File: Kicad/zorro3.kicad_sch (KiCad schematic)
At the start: 13 parts, among them CN1 Zorro3, U1 SN74ABT16543DGGR, U12 74LVC07APW_118, U13 SN74ABT16245ADGGR, U2 SN74ABT16543DGGR, U3 SN74ABT16543DGGR, U6 SN74ABT16543DGGR

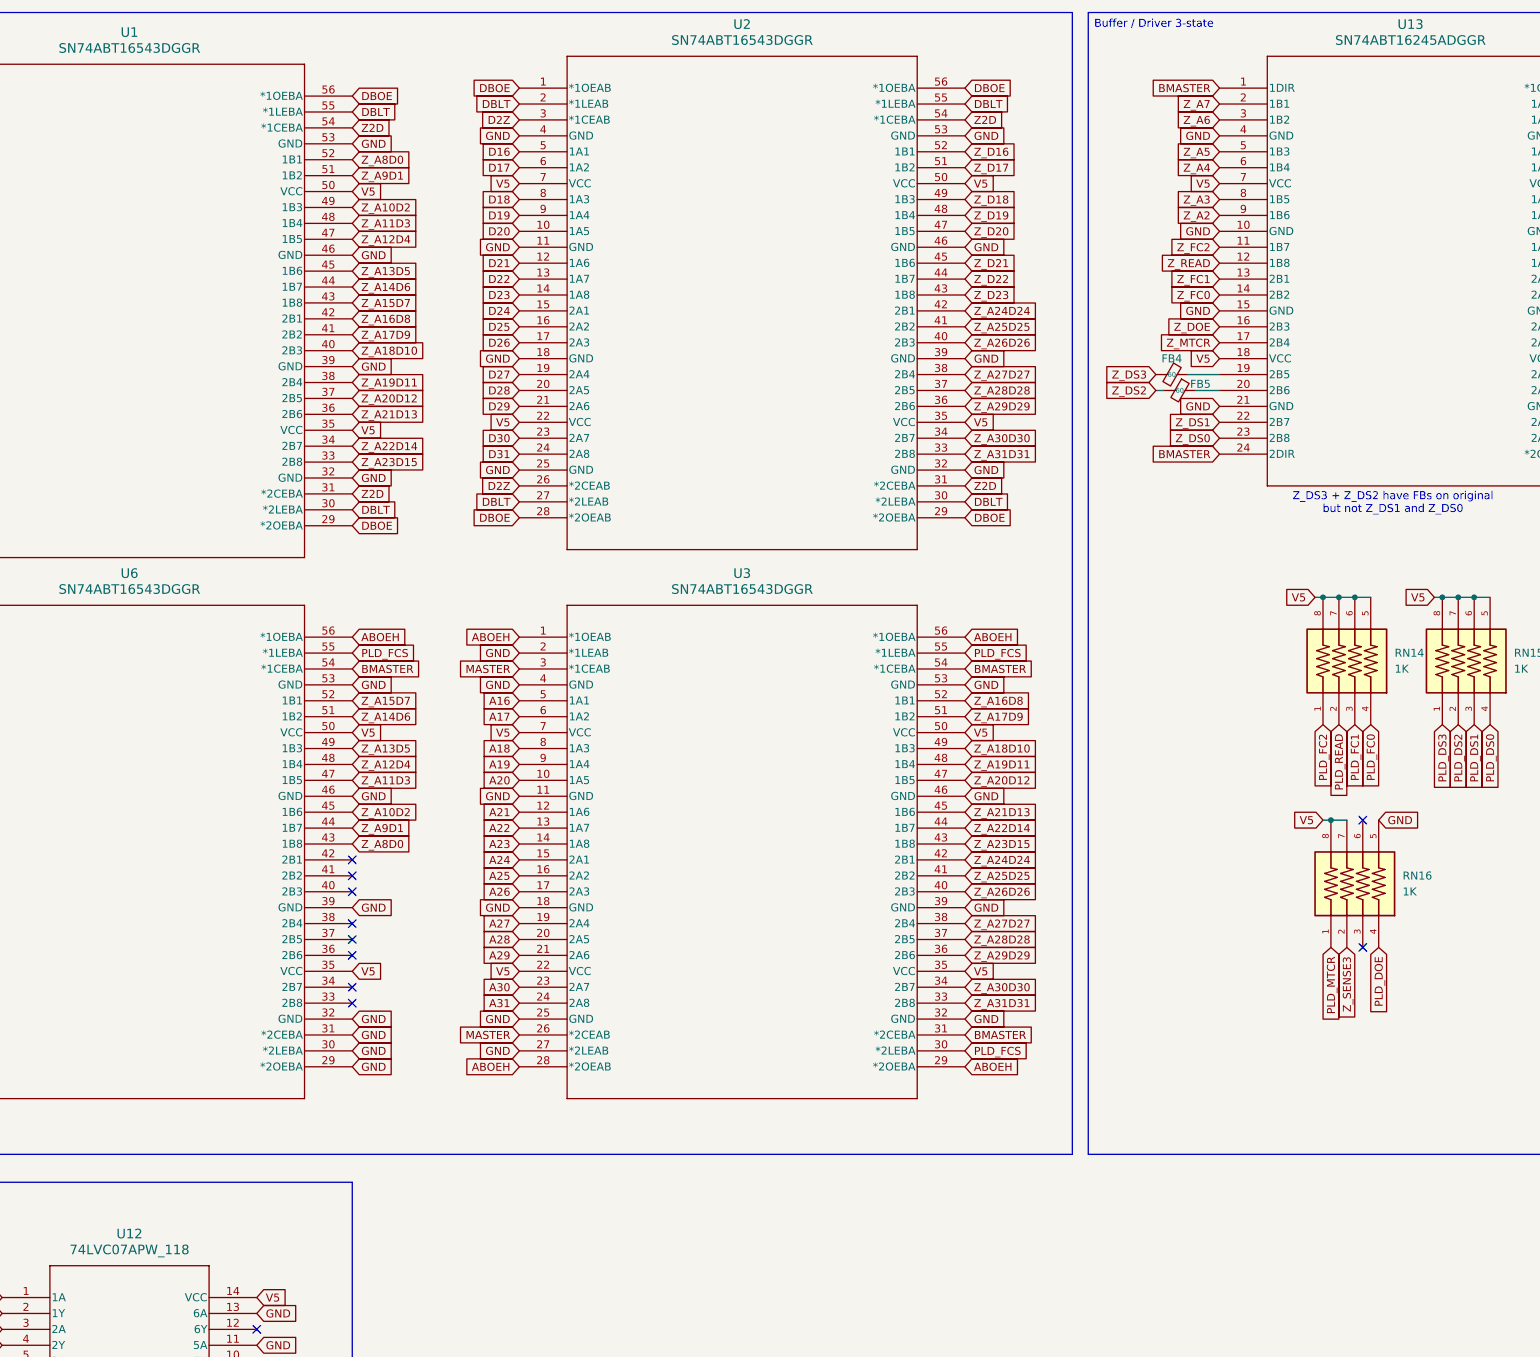
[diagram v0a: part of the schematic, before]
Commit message: Rename all Uxx parts from U1 to U13 for consistency
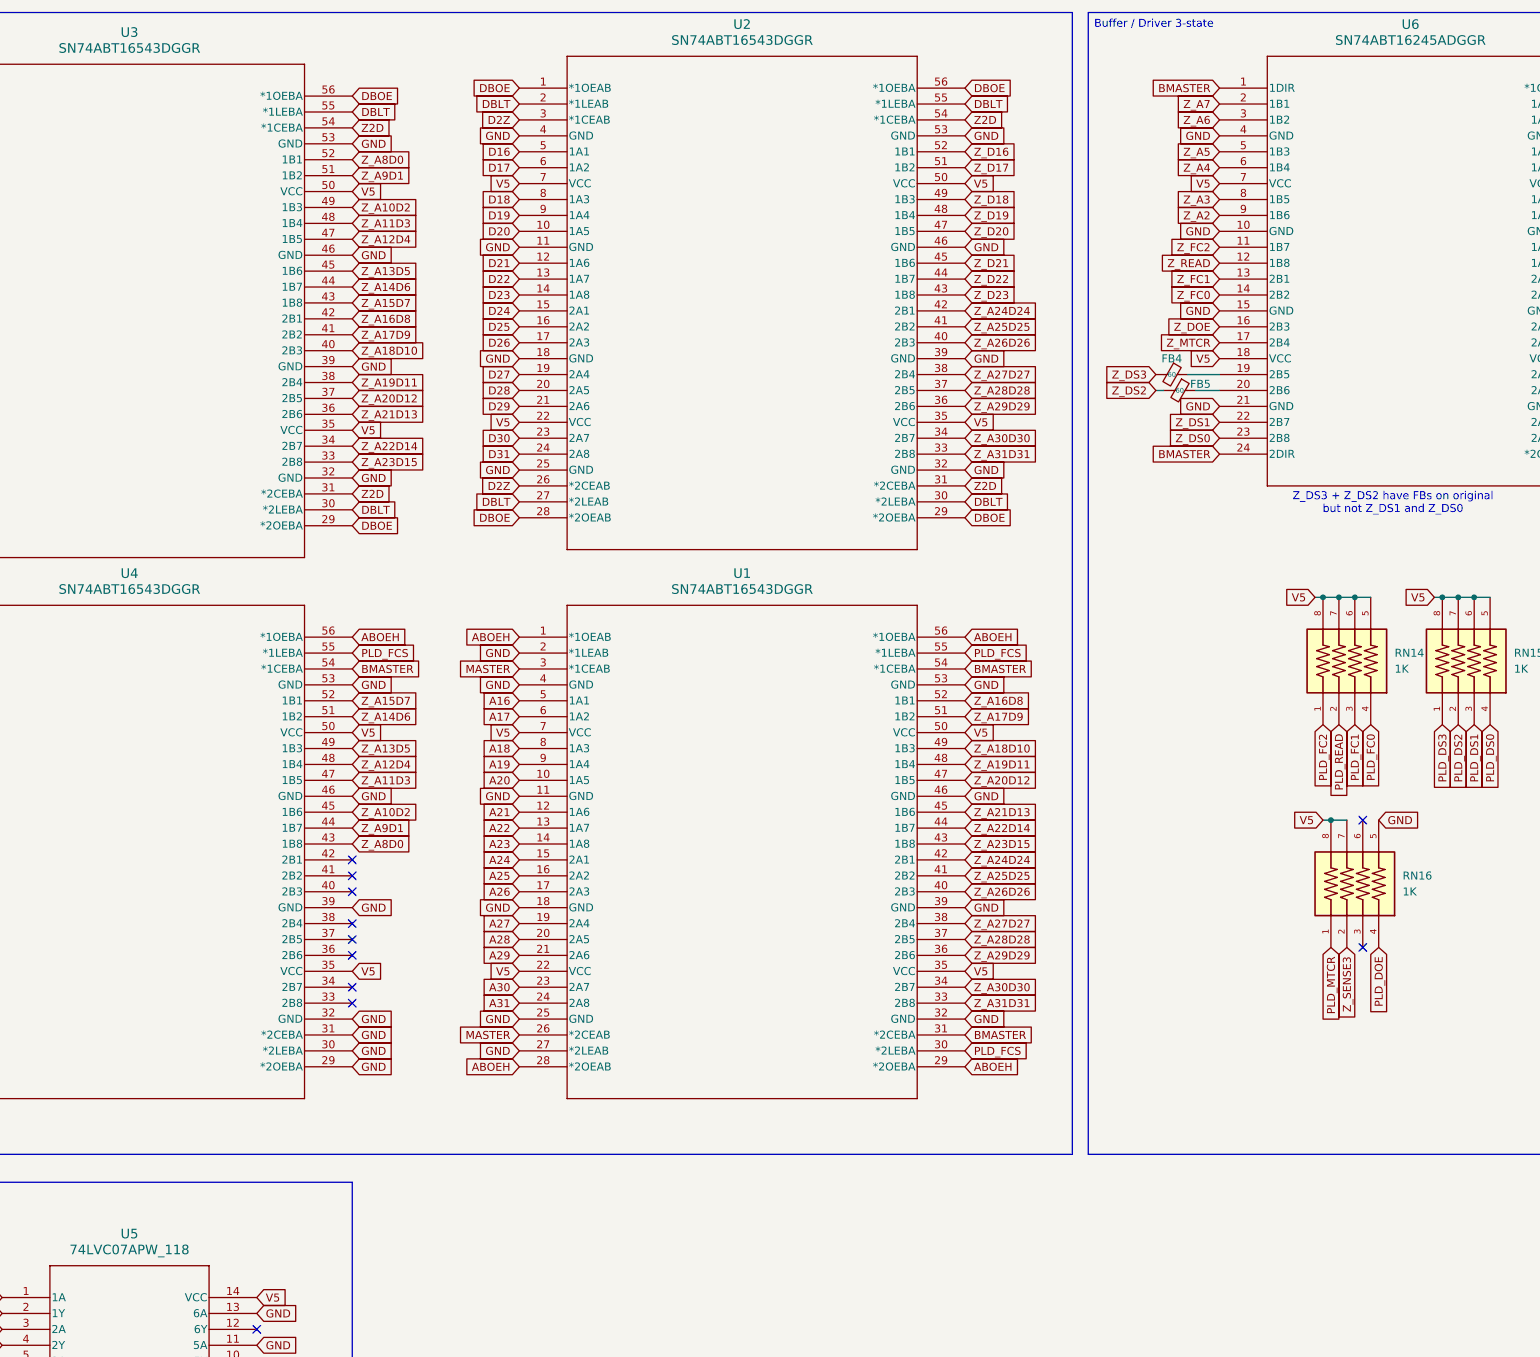
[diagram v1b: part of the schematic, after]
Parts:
- renumbered U3 to U1, U1 to U3, U6 to U4, U12 to U5, U13 to U6
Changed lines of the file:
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@@
 		(dnp no)
 		(fields_autoplaced yes)
-		(property "Reference" "U3"
+		(property "Reference" "U1"
 			(at 161.29 104.14 0)
 			(effects
@@
 			(project ""
 				(path "/8f9f4021-47aa-41d9-bea7-f6ccf72098bb/54ff82a5-3c96-49ab-8139-25683e385401"
-					(reference "U3")
+					(reference "U1")
 					(unit 1)
 				)
@@
 		(dnp no)
 		(fields_autoplaced yes)
-		(property "Reference" "U1"
+		(property "Reference" "U3"
 			(at 63.5 17.78 0)
 			(effects
@@
 			(project ""
 				(path "/8f9f4021-47aa-41d9-bea7-f6ccf72098bb/54ff82a5-3c96-49ab-8139-25683e385401"
-					(reference "U1")
+					(reference "U3")
 					(unit 1)
 				)
@@
 		(dnp no)
 		(fields_autoplaced yes)
-		(property "Reference" "U6"
+		(property "Reference" "U4"
 			(at 63.5 104.14 0)
 			(effects
@@
 			(project "A4092"
 				(path "/8f9f4021-47aa-41d9-bea7-f6ccf72098bb/54ff82a5-3c96-49ab-8139-25683e385401"
-					(reference "U6")
+					(reference "U4")
 					(unit 1)
 				)
@@
 		(dnp no)
 		(fields_autoplaced yes)
-		(property "Reference" "U12"
+		(property "Reference" "U5"
 			(at 63.5 209.55 0)
 			(effects
@@
 			(project ""
 				(path "/8f9f4021-47aa-41d9-bea7-f6ccf72098bb/54ff82a5-3c96-49ab-8139-25683e385401"
-					(reference "U12")
+					(reference "U5")
 					(unit 1)
 				)
@@
 		(dnp no)
 		(fields_autoplaced yes)
-		(property "Reference" "U13"
+		(property "Reference" "U6"
 			(at 267.97 16.51 0)
 			(effects
@@
 			(project ""
 				(path "/8f9f4021-47aa-41d9-bea7-f6ccf72098bb/54ff82a5-3c96-49ab-8139-25683e385401"
-					(reference "U13")
+					(reference "U6")
 					(unit 1)
 				)

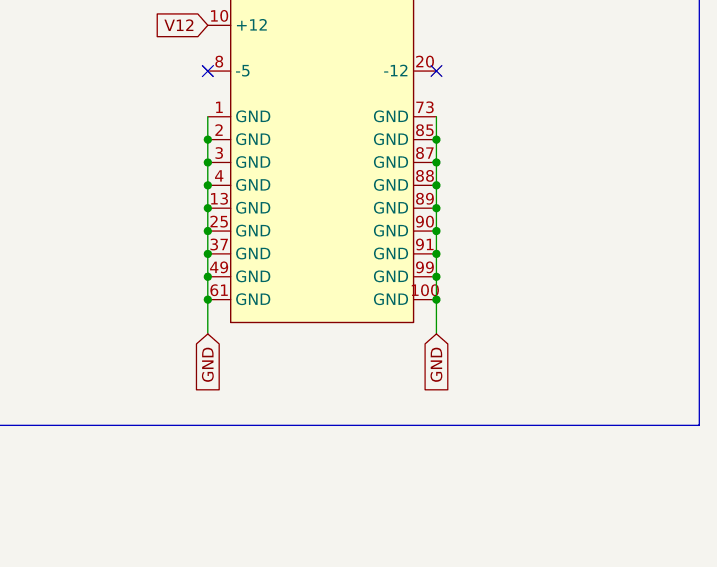
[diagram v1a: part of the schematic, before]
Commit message: Fix Zorro III symbol
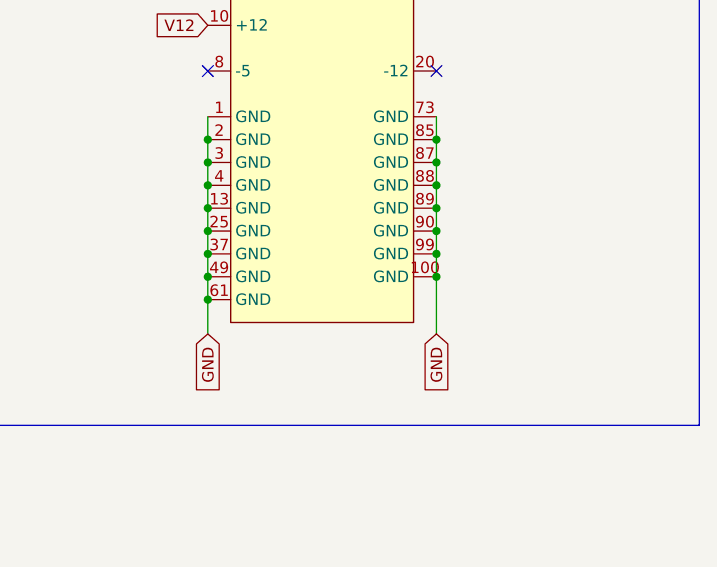
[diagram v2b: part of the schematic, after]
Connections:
- net GND: no longer CN1.91 (GND)
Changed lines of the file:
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@@
 	)
 	(junction
-		(at 370.84 182.88)
-		(diameter 0)
-		(color 0 0 0 0)
-	)
-	(junction
 		(at 370.84 172.72)
 		(diameter 0)
@@
 	(wire
 		(pts
-			(xy 370.84 182.88) (xy 370.84 186.69)
-		)
-		(stroke
-			(width 0)
-			(type default)
-		)
-	)
-	(wire
-		(pts
 			(xy 345.44 180.34) (xy 345.44 182.88)
 		)
@@
 	(wire
 		(pts
-			(xy 370.84 180.34) (xy 370.84 182.88)
+			(xy 370.84 180.34) (xy 370.84 186.69)
 		)
 		(stroke
@@
 	)
 	(symbol
+		(lib_name "Zorro3_1")
 		(lib_id "Zorro3:Zorro3")
 		(at 358.14 166.37 0)
@@
 		(pin "96"
 		)
-		(pin "91"
-		)
 		(pin "36"

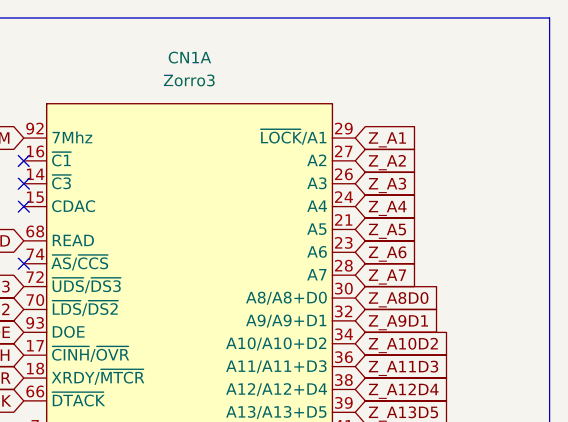
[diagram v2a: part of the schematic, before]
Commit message: Fix Z_LOCK in zorro3 schematics
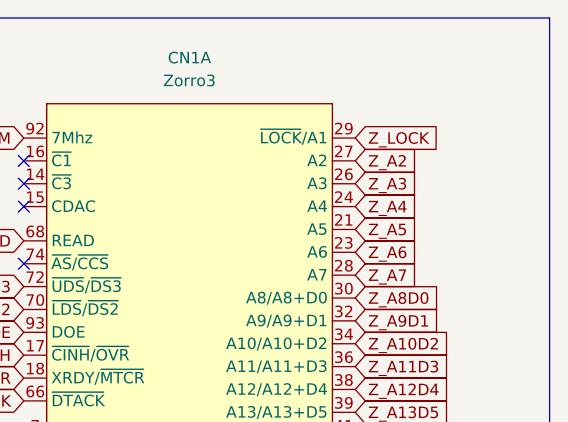
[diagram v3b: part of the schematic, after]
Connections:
- net Z_A1 renamed Z_LOCK
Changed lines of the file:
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@@
 		)
 	)
-	(global_label "Z_A1"
+	(global_label "Z_LOCK"
 		(shape input)
 		(at 378.46 27.94 0)
@@
 		)
 		(property "Intersheetrefs" "${INTERSHEET_REFS}"
-			(at 385.9204 27.94 0)
+			(at 388.5209 27.94 0)
 			(effects
 				(font

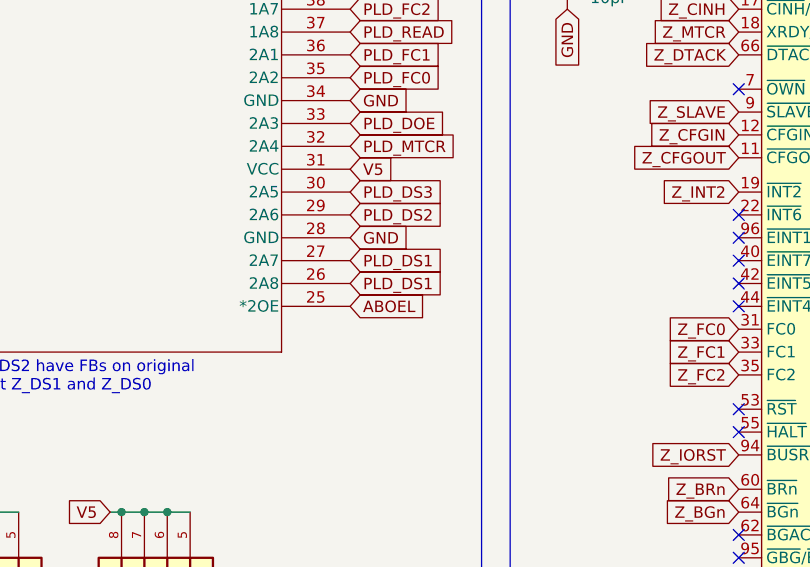
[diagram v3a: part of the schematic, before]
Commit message: This should be PLD_DS0, not PLD_DS1
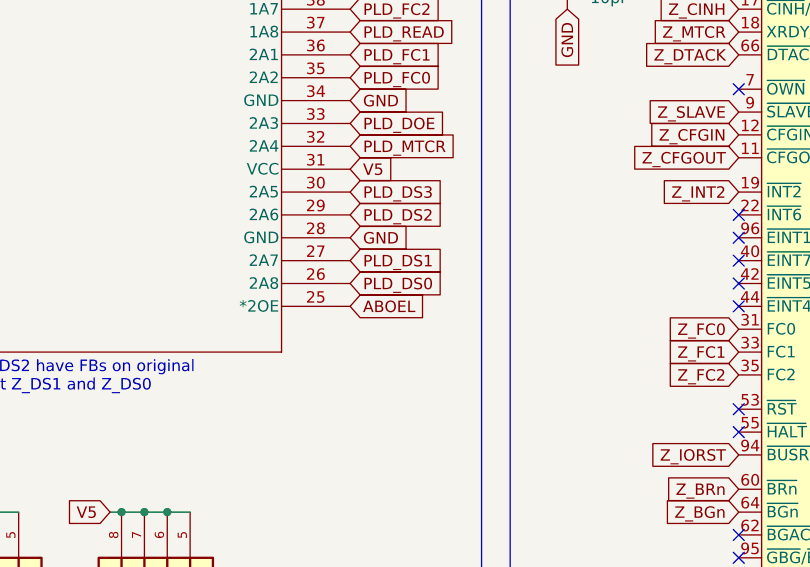
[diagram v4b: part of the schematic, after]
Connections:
- net PLD_DS0: now also U6.26 (2A8)
- net PLD_DS1: no longer U6.26 (2A8)
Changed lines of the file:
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@@
 		)
 	)
-	(global_label "PLD_DS1"
+	(global_label "PLD_DS0"
 		(shape input)
 		(at 298.45 82.55 0)

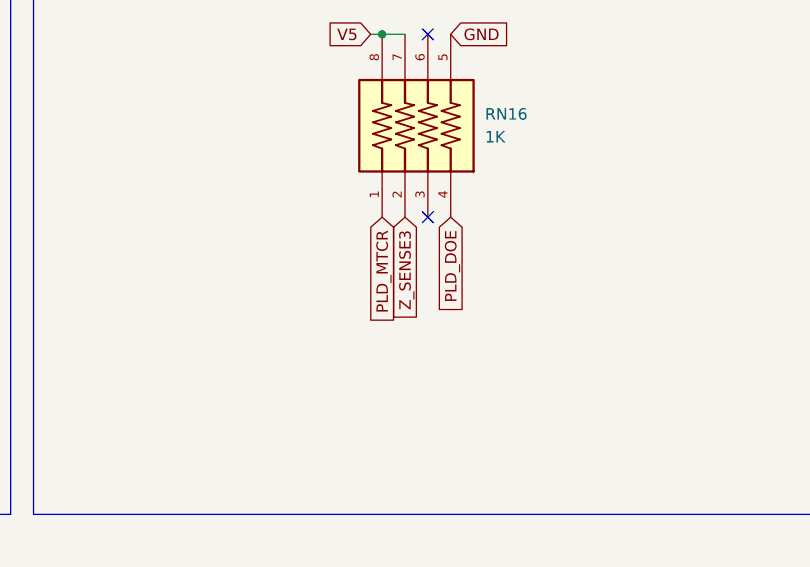
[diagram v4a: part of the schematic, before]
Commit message: Fix various errors from issue #1
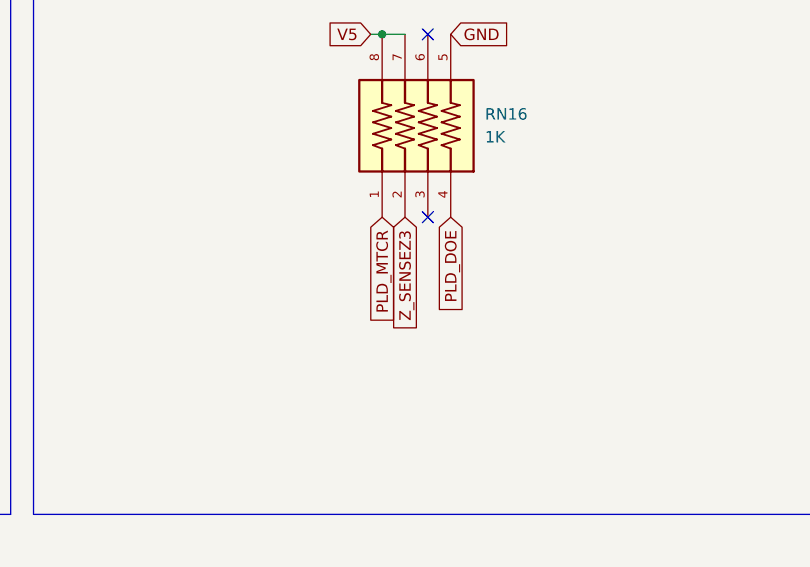
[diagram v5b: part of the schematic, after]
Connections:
- net Z_SENSE3 is gone; now on net Z_SENSEZ3: RN16.2
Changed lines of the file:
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@@
 		)
 	)
-	(global_label "Z_SENSE3"
+	(global_label "Z_SENSEZ3"
 		(shape input)
 		(at 257.81 163.83 270)
@@
 		)
 		(property "Intersheetrefs" "${INTERSHEET_REFS}"
-			(at 257.81 176.2493 90)
+			(at 257.81 177.4588 90)
 			(effects
 				(font

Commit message: Update sheet, add pull down on ROM_CE
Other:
- company: (none) -> amiga.technology
- title: (none) -> A4092
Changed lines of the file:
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@@
 	(generator_version "9.0")
 	(paper "A3")
+	(title_block
+		(title "A4092")
+		(rev "PROTO0")
+		(company "amiga.technology")
+	)
 	(text "Z_DS3 + Z_DS2 have FBs on original\nbut not Z_DS1 and Z_DS0"
 		(exclude_from_sim no)

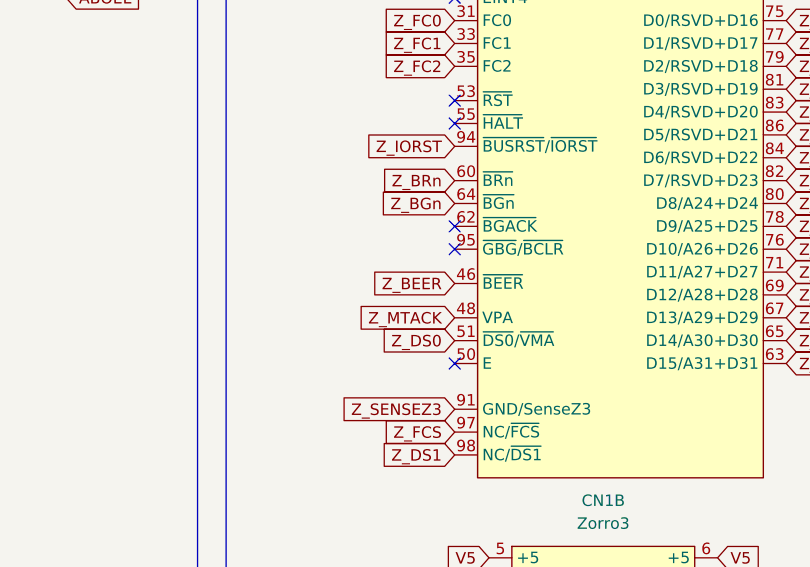
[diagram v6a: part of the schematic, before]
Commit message: Fix issues #12 and #13
Z_BEER and SCSI_BUSY were not connected correctly (single net pins)
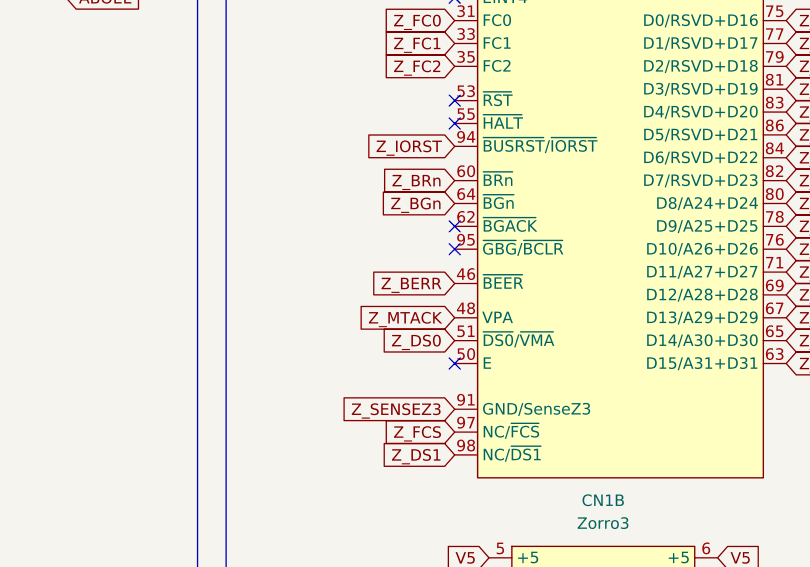
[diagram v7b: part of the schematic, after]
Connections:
- net Z_BEER is gone; now on net Z_BERR: CN1.46 (~{BEER})
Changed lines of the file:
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@@
 		)
 	)
-	(global_label "Z_BEER"
+	(global_label "Z_BERR"
 		(shape input)
 		(at 341.63 116.84 180)
@@
 		)
 		(property "Intersheetrefs" "${INTERSHEET_REFS}"
-			(at 331.6297 116.84 0)
+			(at 331.5087 116.84 0)
 			(effects
 				(font
